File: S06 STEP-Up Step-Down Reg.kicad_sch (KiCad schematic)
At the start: 53 parts, among them Q16 IAUCN04S7L019, Q17 IAUCN04S7L028, Q18 CSD17304Q3, Q19 IAUCN04S7L019, U5 LM51772RHAR

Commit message: New PG-TDSON-8-33 footprint for Q16/Q17/Q19; set SMD/THT types; BON pads to TP
- Q16/Q17/Q19 move to Infineon_PG-TDSON-8-33_5.48x5.15mm_P1.27mm, built from
  the IAUCN04S7L019 datasheet land pattern: centred copper, separate stencil
  apertures (2x2 windows, ~58% on the exposed pad). Pad numbering matches the
  existing symbol (source bar = 1, exposed pad = 8).
- Set the footprint type on 42 untyped imported parts (37 SMD, J1/J2/J4/J5/J6
  through-hole), on the board and in the project library, so they reach the
  SMD position file.
- Rename pogo test pads BON1-26 to TP1-26, exclude them from BOM and position
  files, and point the 0.3 mm pad-to-pad DRC rule at TP*.

DRC: 0 errors, 0 unconnected. ERC: 0 violations.

Co-Authored-By: Claude Opus 5.5 <noreply@anthropic.com>
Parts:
- Q16, Q17, Q19: footprint EVO2513-0_5_0-import-fps:PG-TDSON-8-33 B6.44 x 5.15 H1.0 P1.27 8-Pin EP -> EVO2513-0_5_0-import-fps:Infineon_PG-TDSON-8-33_5.48x5.15mm_P1.27mm
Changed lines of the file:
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@@
 			)
 		)
-		(property "Footprint" "EVO2513-0_5_0-import-fps:PG-TDSON-8-33 B6.44 x 5.15 H1.0 P1.27 8-Pin EP"
+		(property "Footprint" "EVO2513-0_5_0-import-fps:Infineon_PG-TDSON-8-33_5.48x5.15mm_P1.27mm"
 			(at 160.02 83.82 0)
 			(hide yes)
@@
 			)
 		)
-		(property "Footprint" "EVO2513-0_5_0-import-fps:PG-TDSON-8-33 B6.44 x 5.15 H1.0 P1.27 8-Pin EP"
+		(property "Footprint" "EVO2513-0_5_0-import-fps:Infineon_PG-TDSON-8-33_5.48x5.15mm_P1.27mm"
 			(at 250.19 85.09 0)
 			(hide yes)
@@
 			)
 		)
-		(property "Footprint" "EVO2513-0_5_0-import-fps:PG-TDSON-8-33 B6.44 x 5.15 H1.0 P1.27 8-Pin EP"
+		(property "Footprint" "EVO2513-0_5_0-import-fps:Infineon_PG-TDSON-8-33_5.48x5.15mm_P1.27mm"
 			(at 160.02 46.99 0)
 			(hide yes)

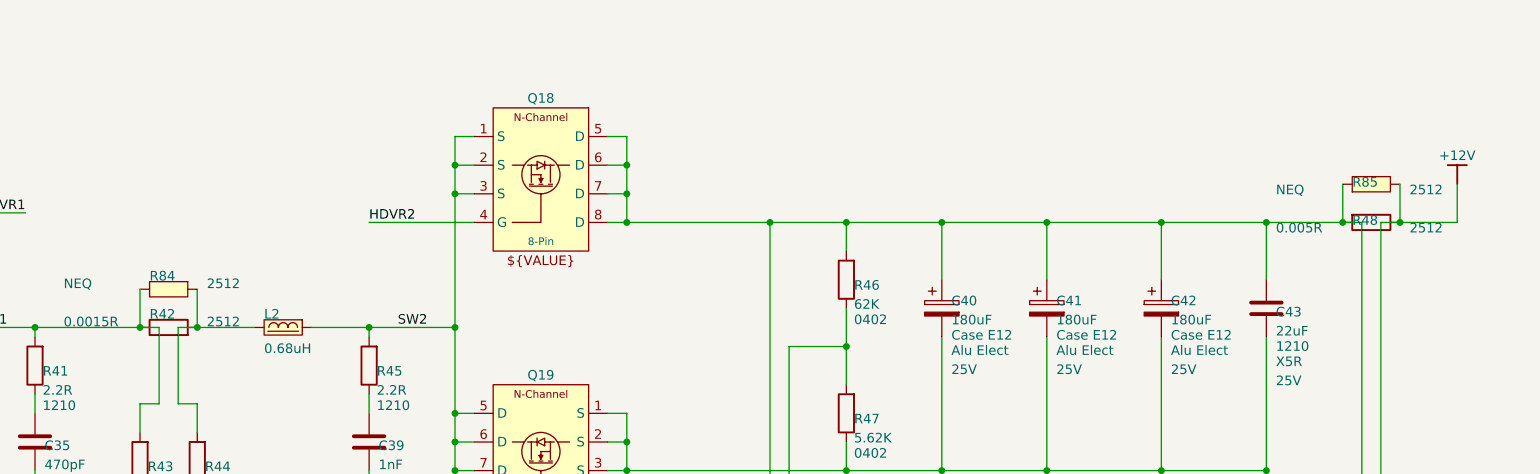
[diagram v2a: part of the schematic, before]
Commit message: U11 PCAL9714HNMP 3D model; FET zone reshaping; R23/R82-R85 DNP
- U11 moves to a project-library copy of HVQFN-24-1EP_4x4mm_P0.5mm_EP2.6x2.6mm
  linked to ${KIPRJMOD}/PCAL9714HNMP.stp (STEP later embedded; file not kept). Schematic and Lattech
  symbol point at the project copy.
- Board updated from the schematic (symbol pin data on the swapped
  footprints) and zone fills reshaped around the FETs.
- R23, R82-R85 (NEQ) set DNP in the schematic and on the board.

DRC: 0 errors, 0 unconnected, 0 schematic parity issues. ERC: 0 violations.

Co-Authored-By: Claude Opus 5.5 <noreply@anthropic.com>
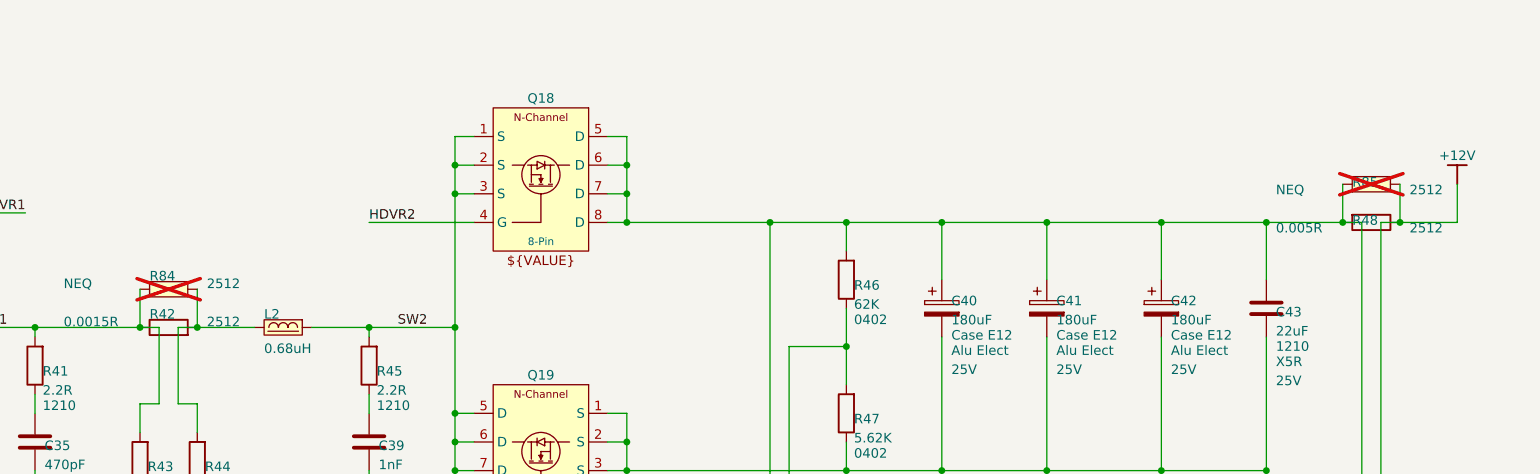
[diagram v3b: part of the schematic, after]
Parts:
- R84, R85: now not fitted
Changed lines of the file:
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@@
 		(on_board yes)
 		(in_pos_files yes)
-		(dnp no)
+		(dnp yes)
 		(property "Reference" "R84"
 			(at 198.12 67.564 0)
@@
 		(on_board yes)
 		(in_pos_files yes)
-		(dnp no)
+		(dnp yes)
 		(property "Reference" "R85"
 			(at 358.14 53.594 0)

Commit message: U5 I2C configuration by default; 10K I2C pull-ups; fix expander port map
- Fit the U5 (LM51772) I2C build: R104-R107 fitted, R38 6.49K -> 0R
  (I2C at 0x6A), R29/R30 DNP. R97/R98 stay unfitted (same J3 pins).
- R106/R107 pull-ups 2.2K -> 10K for slow edges (EMC); limits the bus
  to 100 kHz standard mode.
- Docs and the S08 note: P0_0 drives ENSBC and P0_1 drives nENDAQ
  (active low), matching the routed schematic and board.
- J3.34/J3.36 keep the MCU_ENDAQ/MCU_ENEXT net names.

DRC: 0 errors, 0 unconnected, 0 schematic parity issues. ERC: 0 violations.

Co-Authored-By: Claude Opus 5.5 <noreply@anthropic.com>
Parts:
- R104, R105: now fitted
- R106, R107: value 2.2K -> 10K; ALTIUM_VALUE 2.2K -> 10K; now fitted
- R29, R30: now not fitted
- R38: value 6.49K -> 0R; ALTIUM_VALUE 6.49K -> 0R; MANUFACTURER (none) -> ?; MANUFACTURER_PN (none) -> ?
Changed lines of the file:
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@@
 		(on_board yes)
 		(in_pos_files yes)
-		(dnp yes)
+		(dnp no)
 		(property "Reference" "R106"
 			(at 310.896 190.5 0)
@@
 			)
 		)
-		(property "Value" "2.2K"
+		(property "Value" "10K"
 			(at 310.896 193.04 0)
 			(show_name no)
@@
 			)
 		)
-		(property "Description" "Resistor 2.2K 1% 0402"
+		(property "Description" "Resistor 10K 1% 0402"
 			(at 309.88 190.5 90)
 			(hide yes)
@@
 			)
 		)
-		(property "ALTIUM_VALUE" "2.2K"
+		(property "ALTIUM_VALUE" "10K"
 			(at 308.864 186.182 0)
 			(hide yes)
@@
 		(on_board yes)
 		(in_pos_files yes)
-		(dnp yes)
+		(dnp no)
 		(property "Reference" "R105"
 			(at 318.77 217.424 90)
@@
 		(on_board yes)
 		(in_pos_files yes)
-		(dnp yes)
+		(dnp no)
 		(property "Reference" "R104"
 			(at 318.77 197.104 90)
@@
 		(on_board yes)
 		(in_pos_files yes)
-		(dnp no)
+		(dnp yes)
 		(property "Reference" "R30"
 			(at 63.246 214.63 0)
@@
 		(on_board yes)
 		(in_pos_files yes)
-		(dnp no)
+		(dnp yes)
 		(property "Reference" "R29"
 			(at 53.086 214.63 0)
@@
 		(on_board yes)
 		(in_pos_files yes)
-		(dnp yes)
+		(dnp no)
 		(property "Reference" "R107"
 			(at 310.896 210.82 0)
@@
 			)
 		)
-		(property "Value" "2.2K"
+		(property "Value" "10K"
 			(at 310.896 213.36 0)
 			(show_name no)
@@
 			)
 		)
-		(property "Description" "Resistor 2.2K 1% 0402"
+		(property "Description" "Resistor 10K 1% 0402"
 			(at 309.88 210.82 90)
 			(hide yes)
@@
 			)
 		)
-		(property "ALTIUM_VALUE" "2.2K"
+		(property "ALTIUM_VALUE" "10K"
 			(at 308.864 206.502 0)
 			(hide yes)
@@
 			)
 		)
-		(property "Value" "6.49K"
+		(property "Value" "0R"
 			(at 115.316 217.17 0)
 			(show_name no)
@@
 			)
 		)
-		(property "Description" "Resistor 6.49K 1% 0402"
+		(property "Description" "Resistor 0R 0402"
 			(at 114.3 214.63 90)
 			(hide yes)
@@
 			)
 		)
-		(property "MANUFACTURER" ""
+		(property "MANUFACTURER" "?"
 			(at 113.284 210.312 0)
 			(hide yes)
@@
 			)
 		)
-		(property "MANUFACTURER_PN" ""
+		(property "MANUFACTURER_PN" "?"
 			(at 113.284 210.312 0)
 			(hide yes)
@@
 			)
 		)
-		(property "ALTIUM_VALUE" "6.49K"
+		(property "ALTIUM_VALUE" "0R"
 			(at 113.284 210.312 0)
 			(hide yes)

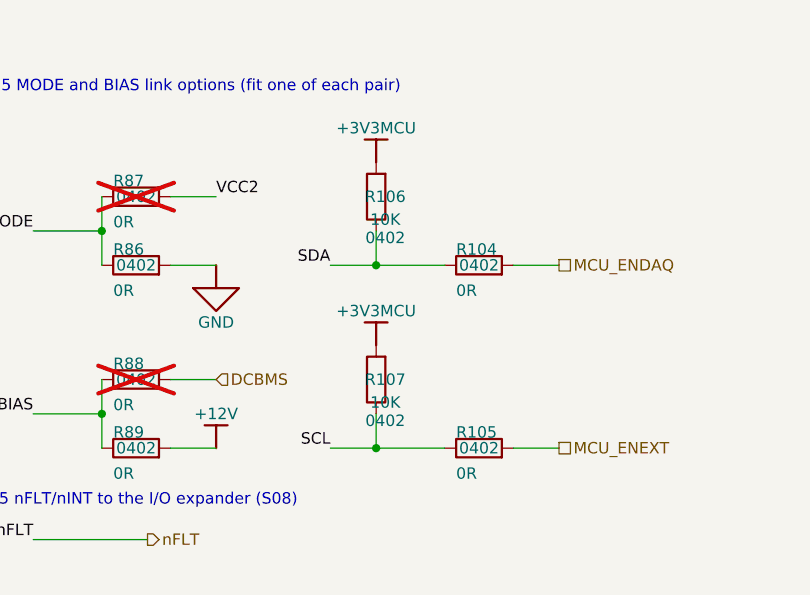
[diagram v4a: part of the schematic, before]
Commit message: Charger rework, 0.5/0.2 mm vias, and current-check vias
- Move and reroute D2, D3, C16, C8 and TH1 in the charger area.
- Change all vias to 0.5 mm pad / 0.2 mm drill.
- Add 33 through vias in the group "Current-check vias". Each one
  continues the rows and columns of the via array next to it. They
  reduce the highest via current at Q17/Q19 GND, SW1, SW2, L2,
  DCSENSED, DCPATH, GDINPUT and +12V (R48/R85).
- Autoplace the reference/value fields on two S06 symbols.

Open DRC error: a GND via at (189.20, 135.60) is 0.074 mm from
the /DCCHARGER track on In6.

Co-Authored-By: Claude Opus 5.5 <noreply@anthropic.com>
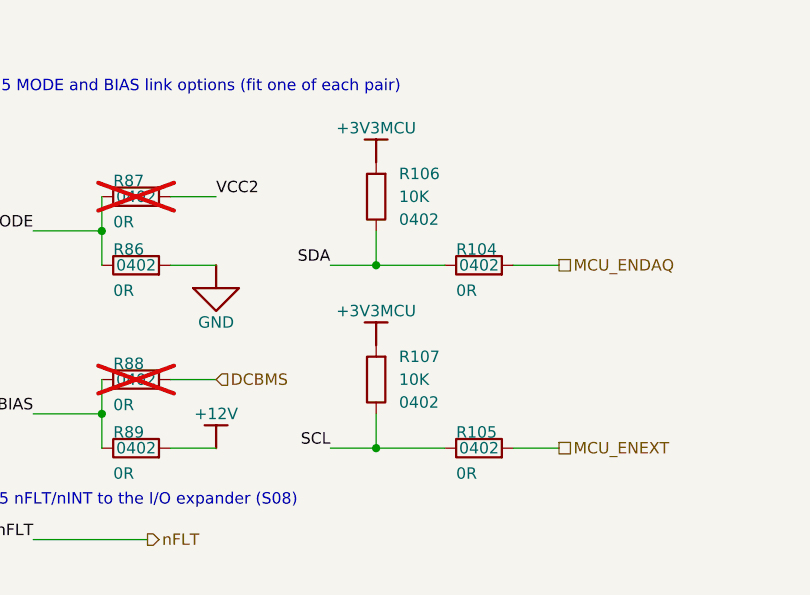
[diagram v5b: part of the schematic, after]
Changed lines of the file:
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@@
 		(in_pos_files yes)
 		(dnp no)
+		(fields_autoplaced yes)
 		(property "Reference" "R106"
-			(at 310.896 190.5 0)
+			(at 312.42 187.9599 0)
 			(show_name no)
 			(do_not_autoplace no)
@@
 					(size 1.27 1.27)
 				)
+				(justify right)
 			)
 		)
 		(property "Value" "10K"
-			(at 310.896 193.04 0)
+			(at 312.42 190.4999 0)
 			(show_name no)
 			(do_not_autoplace no)
@@
 					(size 1.27 1.27)
 				)
+				(justify right)
 			)
 		)
@@
 		)
 		(property "ALTIUM_FOOTPRINT" "0402"
-			(at 310.896 195.072 0)
+			(at 312.42 193.0399 0)
 			(show_name no)
 			(do_not_autoplace no)
@@
 					(size 1.27 1.27)
 				)
+				(justify right)
 			)
 		)
@@
 		(in_pos_files yes)
 		(dnp no)
+		(fields_autoplaced yes)
 		(property "Reference" "R107"
-			(at 310.896 210.82 0)
+			(at 312.42 208.2799 0)
 			(show_name no)
 			(do_not_autoplace no)
@@
 					(size 1.27 1.27)
 				)
+				(justify right)
 			)
 		)
 		(property "Value" "10K"
-			(at 310.896 213.36 0)
+			(at 312.42 210.8199 0)
 			(show_name no)
 			(do_not_autoplace no)
@@
 					(size 1.27 1.27)
 				)
+				(justify right)
 			)
 		)
@@
 		)
 		(property "ALTIUM_FOOTPRINT" "0402"
-			(at 310.896 215.392 0)
+			(at 312.42 213.3599 0)
 			(show_name no)
 			(do_not_autoplace no)
@@
 					(size 1.27 1.27)
 				)
+				(justify right)
 			)
 		)

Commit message: Fix J3 and Q16/Q17/Q19 part numbers; stackup to the fab drawing
- J3 MANUFACTURER_PN 10144517-042802LF -> 10144517-043802LF, matching
  its value and footprint. The wrong number came from the Altium part
  list.
- Q16/Q19 IAUCN04S7L019ATMA1 and Q17 IAUCN04S7L028ATMA1 in place of
  the package name PG-TDSON-8-33; manufacturer "Infenion" -> Infineon.
- PCB stackup set to the Altium fab drawing: 0.25 mm cores, 2116
  prepregs (doubled between In2/In3 and In4/In5), 0.035 mm outer and
  0.030 mm inner copper, 0.013 mm mask, ENIG. 1.59 mm laminate,
  1.598 mm finished.
- Stackup drawing: second layer label "L1" -> "L2".

Co-Authored-By: Claude Opus 5.5 <noreply@anthropic.com>
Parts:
- Q16, Q19: MANUFACTURER Infenion -> Infineon; MANUFACTURER_PN PG-TDSON-8-33 -> IAUCN04S7L019ATMA1
- Q17: MANUFACTURER_PN PG-TDSON-8-33 -> IAUCN04S7L028ATMA1
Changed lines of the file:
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@@
 			)
 		)
-		(property "MANUFACTURER_PN" "PG-TDSON-8-33"
+		(property "MANUFACTURER_PN" "IAUCN04S7L028ATMA1"
 			(at 159.512 77.47 0)
 			(hide yes)
@@
 			)
 		)
-		(property "MANUFACTURER" "Infenion"
+		(property "MANUFACTURER" "Infineon"
 			(at 249.682 78.74 0)
 			(hide yes)
@@
 			)
 		)
-		(property "MANUFACTURER_PN" "PG-TDSON-8-33"
+		(property "MANUFACTURER_PN" "IAUCN04S7L019ATMA1"
 			(at 249.682 78.74 0)
 			(hide yes)
@@
 			)
 		)
-		(property "MANUFACTURER" "Infenion"
+		(property "MANUFACTURER" "Infineon"
 			(at 159.512 40.64 0)
 			(hide yes)
@@
 			)
 		)
-		(property "MANUFACTURER_PN" "PG-TDSON-8-33"
+		(property "MANUFACTURER_PN" "IAUCN04S7L019ATMA1"
 			(at 159.512 40.64 0)
 			(hide yes)
